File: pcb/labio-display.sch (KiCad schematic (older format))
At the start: 5 parts, among them P401 CONN_01X12, SW401 DIP_SWITCH_X04

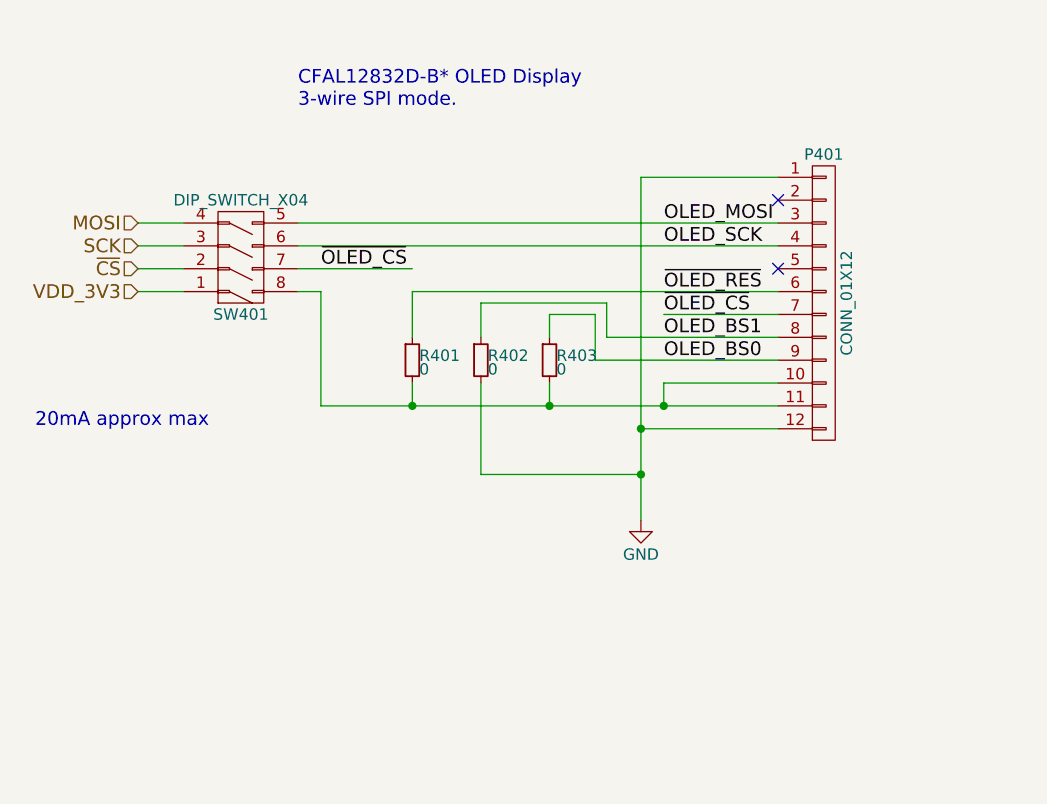
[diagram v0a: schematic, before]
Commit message: expand outline to 175x85mm. move screen zif connector to top
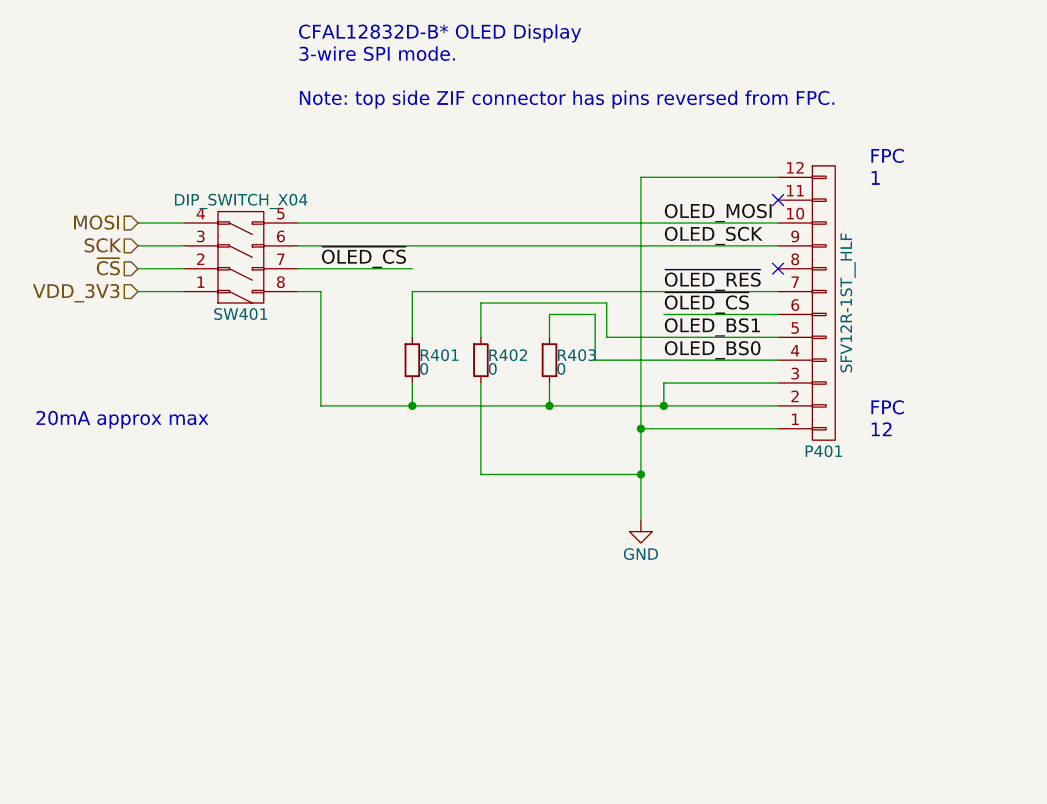
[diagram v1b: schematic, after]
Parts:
- P401: value CONN_01X12 -> SFV12R-1ST__HLF
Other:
- note added: "CFAL12832D-B* OLED Display\n3-wire SPI mode.\n\nNote: top side ZIF connector has pins reversed from FPC."
- note added: "FPC\n1"
- note added: "FPC\n12"
- note removed: "CFAL12832D-B* OLED Display\n3-wire SPI mode."
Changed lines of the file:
@@
 P 6800 2950
 F 0 "P401" H 6800 3600 50  0000 C CNN
-F 1 "CONN_01X12" V 6900 2950 50  0000 C CNN
+F 1 "SFV12R-1ST__HLF" V 6900 2950 50  0000 C CNN
 F 2 "labio-special:SFVxxR-xSTxxHLF" H 6800 2950 50  0001 C CNN
 F 3 "" H 6800 2950 50  0000 C CNN
 	1    6800 2950
-	1    0    0    -1
+	1    0    0    1
 $EndComp
 Text Notes 4500 2100 0    60   ~ 0
-CFAL12832D-B* OLED Display\n3-wire SPI mode.
+CFAL12832D-B* OLED Display\n3-wire SPI mode.\n\nNote: top side ZIF connector has pins reversed from FPC.
 $Comp
 L GND #PWR09
@@
 03 00 00 00 00 F4 24 84 F2 00 00 00 00 00 3D 09 A1 3C 00 00 00 00 40 4F 42 28 0F 00 00 00 00 D0
 93 10 CA 03 00 00 00 00 F4 24 84 F2 00 00 00 00 00 3D 09 A1 3C 00 00 00 00 40 4F FA 3F 4E 16 A4
-A2 80 4C E9 AA 00 00 00 00 49 45 4E 44 AE 42 60 82 3B
+A2 80 4C E9 AA 00 00 00 00 49 45 4E 44 AE 42 60 82 00
 EndData
 $EndBitmap
@@
 Text Label 6100 2900 0    60   ~ 0
 ~OLED_RES
+Text Notes 7000 2450 0    60   ~ 0
+FPC\n1
+Text Notes 7000 3550 0    60   ~ 0
+FPC\n12
 $EndSCHEMATC

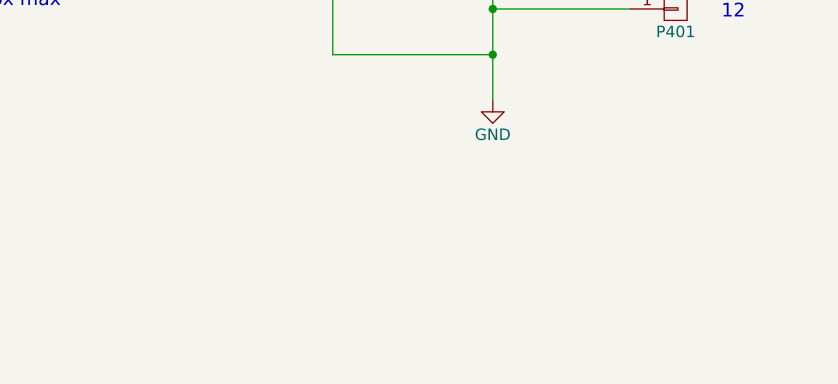
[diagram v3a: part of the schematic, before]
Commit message: Fix board/bom errors from initial build
* Accelerometer (U501) footprint mirrored. Redraw footprint and adjust routing.
* Gyro (U505) footprint mirrored. Redraw footprint and adjust routing.
* Codec (U702) labed as wrong chip. Says WM8731 but should be 8750. Also fix in BOM.
* Should include OLED screen in BOM (not just the connector).
* Codec to TRRS caps have incorrect value. Says 220uF but should be 220pF.
* Mark RPi Hat EEPROM circuit as depopulated in schematic.
* Remove dangling trace near encoder headers.
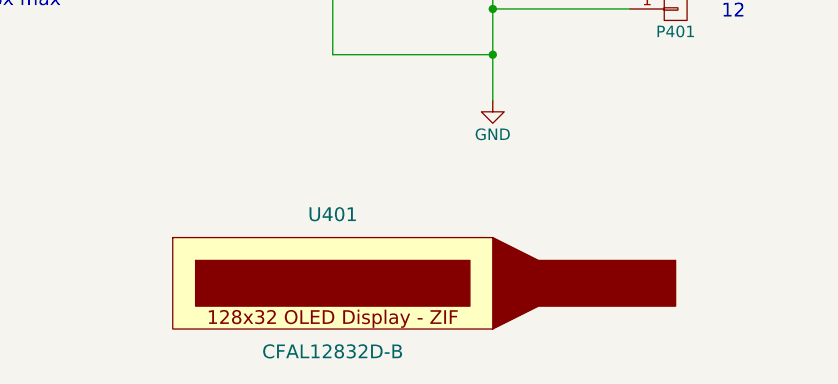
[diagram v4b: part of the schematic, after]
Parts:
- added U401: CFAL12832D-B, symbol CFAL12832D-B
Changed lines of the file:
@@
 CFAL12832D-B* OLED Display\n3-wire SPI mode.\n\nNote: top side ZIF connector has pins reversed from FPC.
 $Comp
-L GND #PWR09
+L GND #PWR401
 U 1 1 575D4D1A
 P 6000 3900
-F 0 "#PWR09" H 6000 3650 50  0001 C CNN
+F 0 "#PWR401" H 6000 3650 50  0001 C CNN
 F 1 "GND" H 6000 3750 50  0000 C CNN
 F 2 "" H 6000 3900 50  0000 C CNN
@@
 Text Notes 7000 3550 0    60   ~ 0
 FPC\n12
+$Comp
+L CFAL12832D-B U401
+U 1 1 579E71CE
+P 5300 4700
+F 0 "U401" H 5300 5000 60  0000 C CNN
+F 1 "CFAL12832D-B" H 5300 4400 60  0000 C CNN
+F 2 "" H 5300 4700 60  0001 C CNN
+F 3 "" H 5300 4700 60  0000 C CNN
+	1    5300 4700
+	1    0    0    -1
+$EndComp
 $EndSCHEMATC
